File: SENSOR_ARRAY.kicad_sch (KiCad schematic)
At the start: 44 parts, among them J2 FH34SRJ-8S-0.5SH_50_, Q1 MMBT3904, U10 QRE1113GR, U11 QRE1113GR, U12 QRE1113GR, U13 QRE1113GR, U14 QRE1113GR, U15 QRE1113GR, U16 QRE1113GR, U17 QRE1113GR, U18 QRE1113GR, U19 QRE1113GR, U4 QRE1113GR, U5 QRE1113GR, U6 QRE1113GR, U7 QRE1113GR, U8 QRE1113GR, U9 QRE1113GR

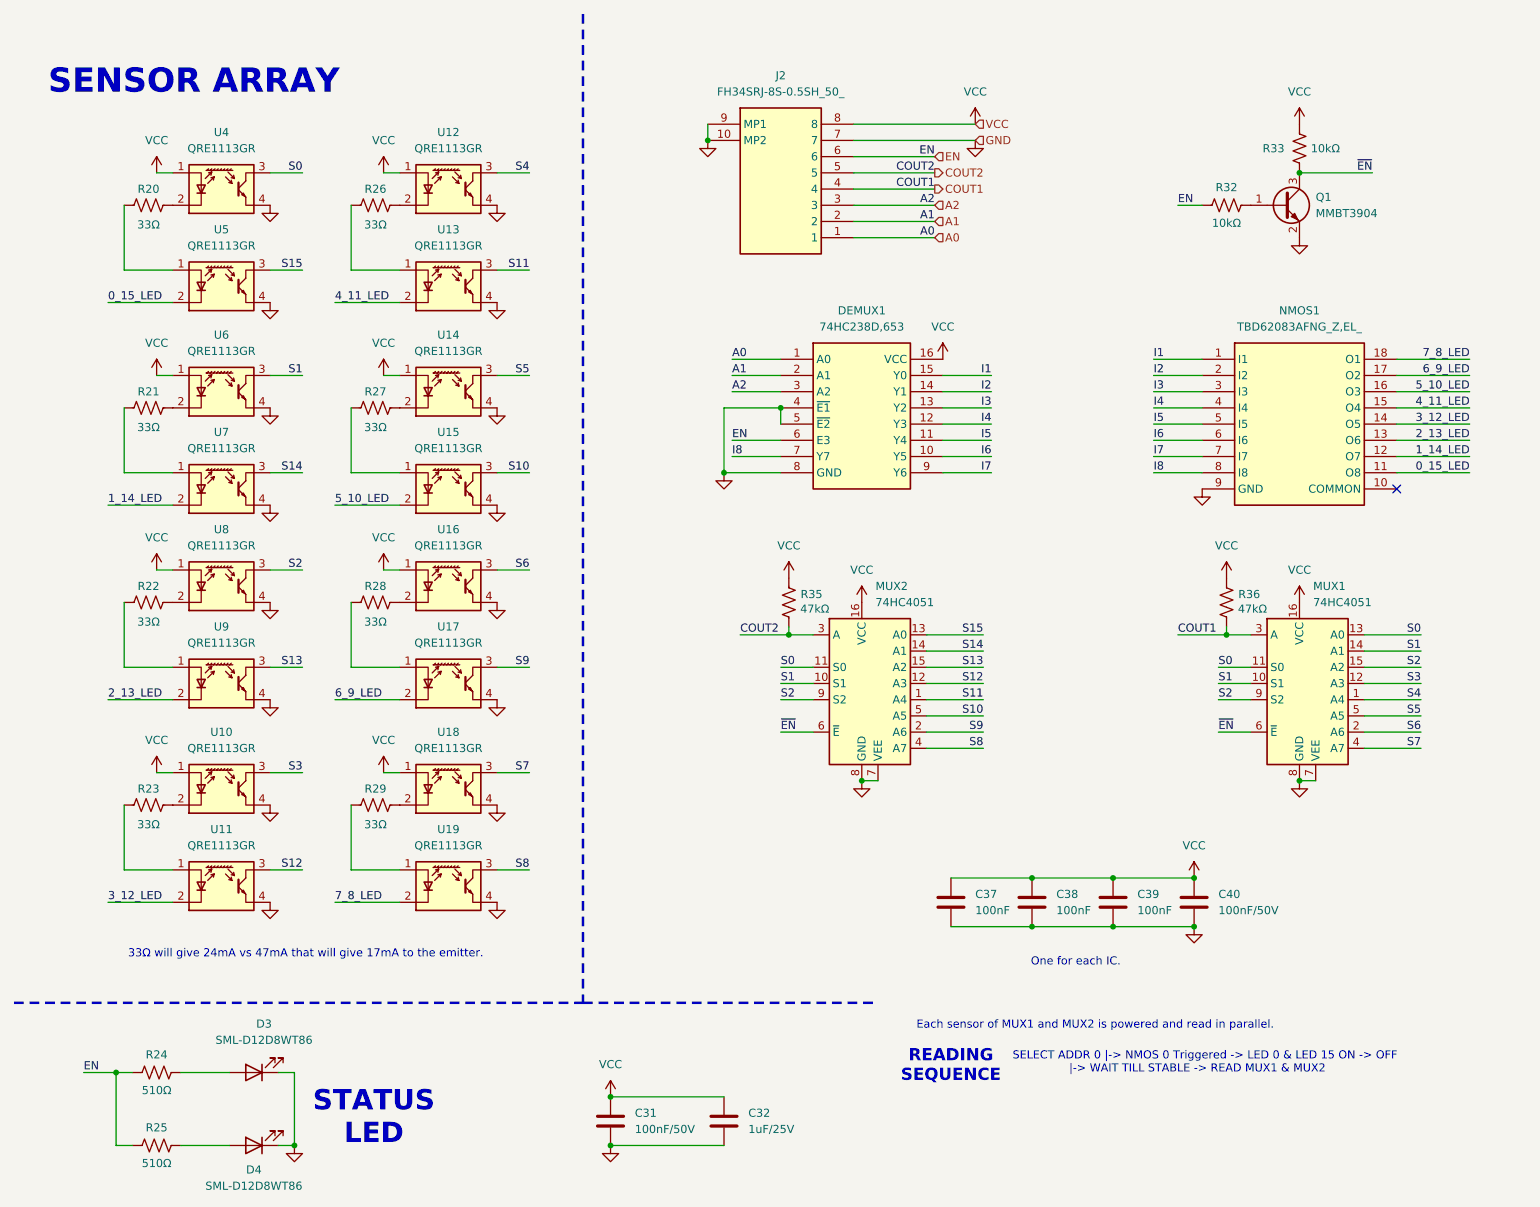
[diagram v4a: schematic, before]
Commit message: Added 3D models to third party footprints. Final Teensy version, switching to SAMD51 custom setup. Please add tag.
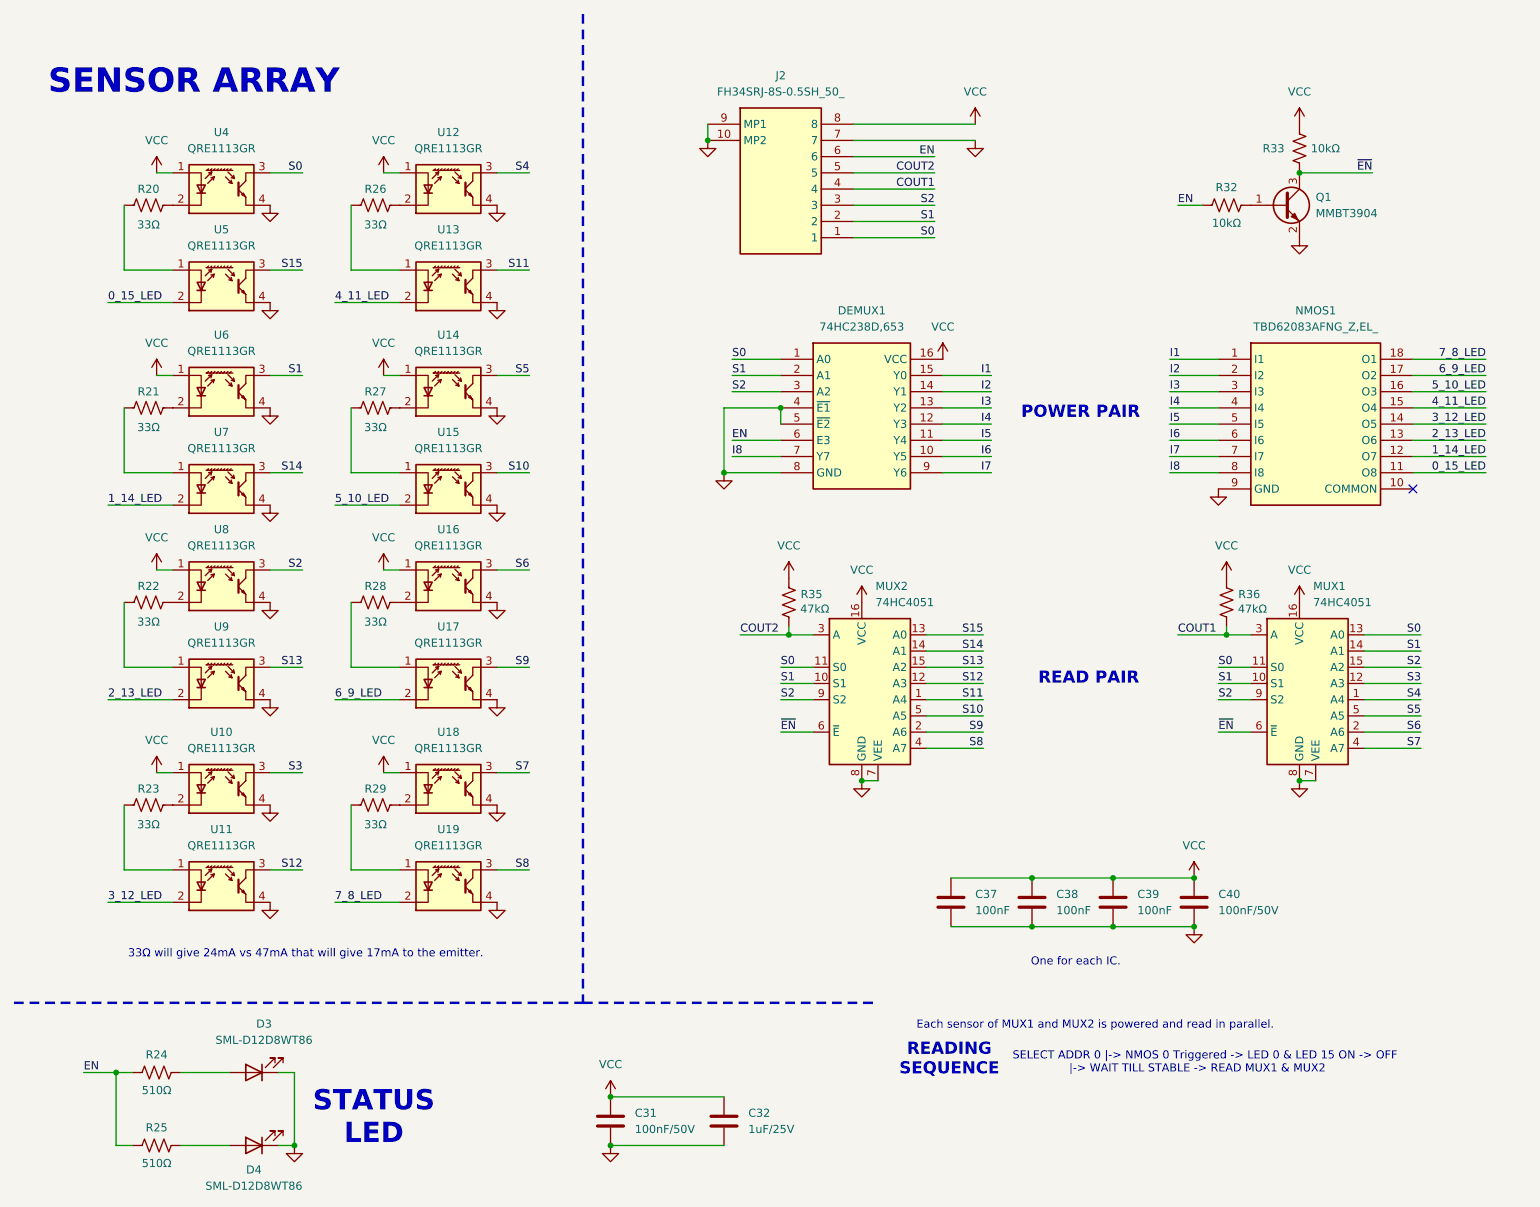
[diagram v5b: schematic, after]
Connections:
- net A0 is gone; now on net S0: DEMUX1.1 (A0), J2.1
- net A1 is gone; now on net S1: DEMUX1.2 (A1), J2.2
- net A2 is gone; now on net S2: DEMUX1.3 (A2), J2.3
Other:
- note added: "POWER PAIR"
- note added: "READ PAIR"
- moved on the sheet: NMOS1

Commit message: Made passives smaller from 0603 to 0402 because I will solder them with hot air gun anyway. Started positioning SAMD51 bypass caps.
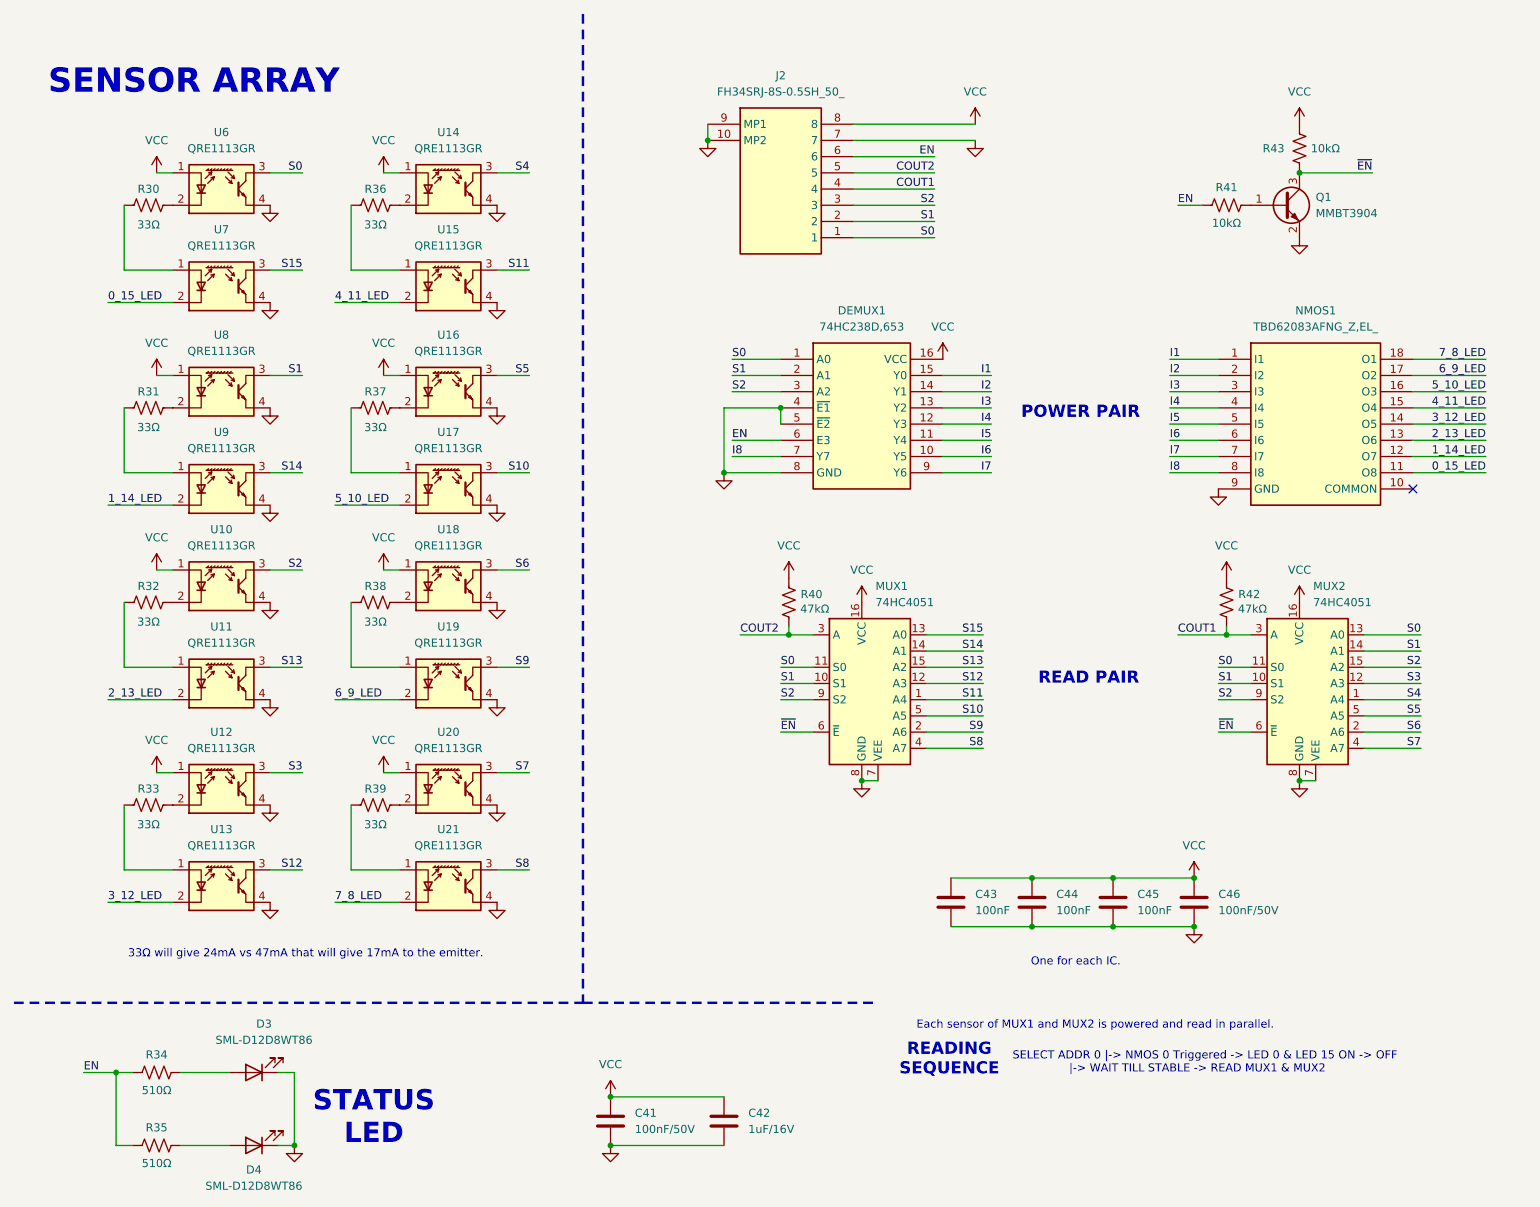
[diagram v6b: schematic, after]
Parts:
- C41: renamed from C31; footprint Capacitor_SMD:C_0603_1608Metric -> Capacitor_SMD:C_0402_1005Metric
- C42: renamed from C32; value 1uF/25V -> 1uF/16V; footprint Capacitor_SMD:C_0603_1608Metric -> Capacitor_SMD:C_0402_1005Metric
- C43: renamed from C37; footprint Capacitor_SMD:C_0603_1608Metric -> Capacitor_SMD:C_0402_1005Metric
- C44: renamed from C38; footprint Capacitor_SMD:C_0603_1608Metric -> Capacitor_SMD:C_0402_1005Metric
- C45: renamed from C39; footprint Capacitor_SMD:C_0603_1608Metric -> Capacitor_SMD:C_0402_1005Metric
- C46: renamed from C40; footprint Capacitor_SMD:C_0603_1608Metric -> Capacitor_SMD:C_0402_1005Metric
- R30: renamed from R20; footprint Resistor_SMD:R_0603_1608Metric -> Resistor_SMD:R_0402_1005Metric
- R31: renamed from R21; footprint Resistor_SMD:R_0603_1608Metric -> Resistor_SMD:R_0402_1005Metric
- R32: renamed from R22; footprint Resistor_SMD:R_0603_1608Metric -> Resistor_SMD:R_0402_1005Metric
- R33: renamed from R23; footprint Resistor_SMD:R_0603_1608Metric -> Resistor_SMD:R_0402_1005Metric
- R34: renamed from R24; footprint Resistor_SMD:R_0603_1608Metric -> Resistor_SMD:R_0402_1005Metric
- R35: renamed from R25; footprint Resistor_SMD:R_0603_1608Metric -> Resistor_SMD:R_0402_1005Metric
- R36: renamed from R26; footprint Resistor_SMD:R_0603_1608Metric -> Resistor_SMD:R_0402_1005Metric
- R37: renamed from R27; footprint Resistor_SMD:R_0603_1608Metric -> Resistor_SMD:R_0402_1005Metric
- R38: renamed from R28; footprint Resistor_SMD:R_0603_1608Metric -> Resistor_SMD:R_0402_1005Metric
- R39: renamed from R29; footprint Resistor_SMD:R_0603_1608Metric -> Resistor_SMD:R_0402_1005Metric
- R40: renamed from R35; footprint Resistor_SMD:R_0603_1608Metric -> Resistor_SMD:R_0402_1005Metric
- R41: renamed from R32; footprint Resistor_SMD:R_0603_1608Metric -> Resistor_SMD:R_0402_1005Metric
- R42: renamed from R36; footprint Resistor_SMD:R_0603_1608Metric -> Resistor_SMD:R_0402_1005Metric
- R43: renamed from R33; footprint Resistor_SMD:R_0603_1608Metric -> Resistor_SMD:R_0402_1005Metric
- renumbered MUX2 to MUX1, MUX1 to MUX2, U8 to U10, U9 to U11, U10 to U12, U11 to U13, U12 to U14, U13 to U15, U14 to U16, U15 to U17, U16 to U18, U17 to U19, U18 to U20, U19 to U21, U4 to U6, U5 to U7, U6 to U8, U7 to U9
